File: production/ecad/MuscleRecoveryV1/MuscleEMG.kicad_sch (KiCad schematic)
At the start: 47 parts, among them J1 AudioJack3, J2 Screw_Terminal_01x03, J8 Screw_Terminal_01x07, U4 ADXL343, U5 AD8232ACPZ-R7, U7 ADS1115IDGS

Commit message: updated bom
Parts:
- C20, C21: footprint (none) -> Capacitor_SMD:C_0805_2012Metric
- R27, R65: footprint (none) -> Resistor_SMD:R_0805_2012Metric
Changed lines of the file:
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@@
       (effects (font (size 1.27 1.27)) (justify left))
     )
-    (property "Footprint" "" (at 149.86 146.05 0)
+    (property "Footprint" "Capacitor_SMD:C_0805_2012Metric" (at 149.86 146.05 0)
       (effects (font (size 1.27 1.27)) hide)
     )
@@
       (effects (font (size 1.27 1.27)) (justify left))
     )
-    (property "Footprint" "" (at 134.62 146.05 0)
+    (property "Footprint" "Capacitor_SMD:C_0805_2012Metric" (at 134.62 146.05 0)
       (effects (font (size 1.27 1.27)) hide)
     )
@@
     )
     (pin "1")
+    (pin "10")
+    (pin "11")
+    (pin "12")
+    (pin "13")
+    (pin "14")
+    (pin "2")
+    (pin "3")
+    (pin "4")
+    (pin "5")
+    (pin "6")
     (pin "7")
     (pin "8")
-    (pin "10")
-    (pin "2")
-    (pin "5")
     (pin "9")
-    (pin "13")
-    (pin "4")
-    (pin "14")
-    (pin "12")
-    (pin "11")
-    (pin "6")
-    (pin "3")
     (instances
       (project "MuscleRecoveryV1"
@@
       (effects (font (size 1.27 1.27)))
     )
-    (property "Footprint" "" (at 115.57 175.768 90)
+    (property "Footprint" "Resistor_SMD:R_0805_2012Metric" (at 115.57 175.768 90)
       (effects (font (size 1.27 1.27)) hide)
     )
@@
       (effects (font (size 1.27 1.27)))
     )
-    (property "Footprint" "" (at 115.57 173.228 90)
+    (property "Footprint" "Resistor_SMD:R_0805_2012Metric" (at 115.57 173.228 90)
       (effects (font (size 1.27 1.27)) hide)
     )
@@
       (effects (font (size 1.27 1.27)) hide)
     )
-    (pin "2")
-    (pin "1")
-    (instances
-      (project "MuscleRecoveryV1"
+    (pin "1")
+    (pin "2")
+    (instances
+      (project "MuscleRecoveryV1"

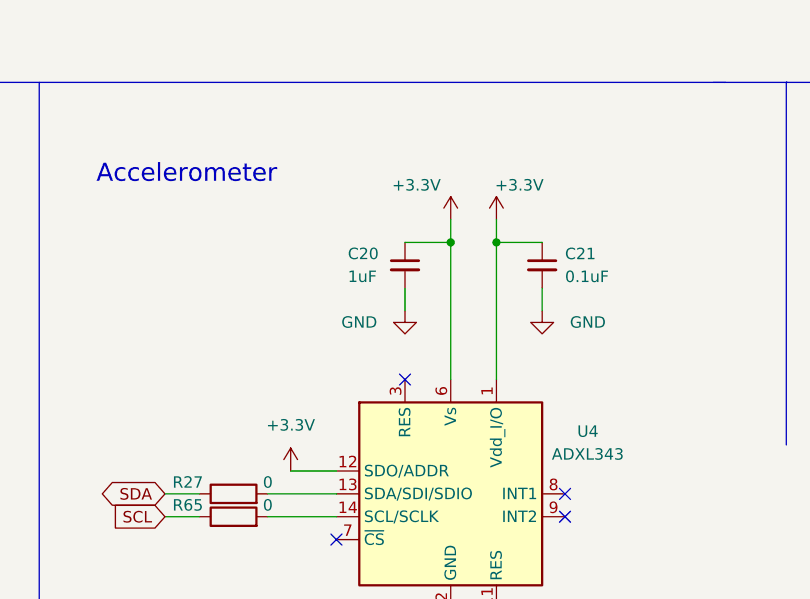
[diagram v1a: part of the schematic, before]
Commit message: added accelerometer to layout
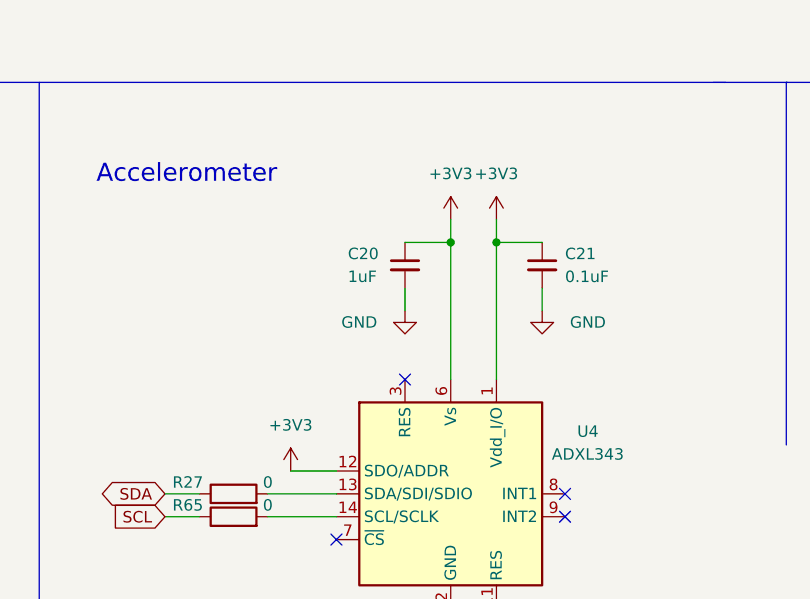
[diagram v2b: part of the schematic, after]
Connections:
- net +3.3V is gone; now on net +3V3: C20.1, C21.1, U4.1 (Vdd_I/O), U4.12 (SDO/ADDR), U4.6 (Vs)
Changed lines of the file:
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@@
-    )
-  )
-  (symbol (lib_id "power:+3.3V") (at 144.78 140.97 0) (unit 1)
-    (in_bom yes) (on_board yes) (dnp no)
-    (property "Reference" "#PWR073" (at 144.78 144.78 0)
-      (effects (font (size 1.27 1.27)) hide)
-    )
-    (property "Value" "+3.3V" (at 147.32 137.16 0)
-      (effects (font (size 1.27 1.27)))
-    )
-    (property "Footprint" "" (at 144.78 140.97 0)
-      (effects (font (size 1.27 1.27)) hide)
-    )
-    (property "Datasheet" "" (at 144.78 140.97 0)
-      (effects (font (size 1.27 1.27)) hide)
-    )
-    (pin "1")
-    (instances
-      (project "MuscleRecoveryV1"
-        (path "/4e550305-79d2-4e4a-a502-817ebcc79f9a/284c60dd-e199-4b03-b99f-cc7eaed256f8"
-          (reference "#PWR073") (unit 1)
-        )
-      )
     )
   )
@@
     )
   )
+  (symbol (lib_id "power:+3V3") (at 144.78 140.97 0) (unit 1)
+    (in_bom yes) (on_board yes) (dnp no) (fields_autoplaced)
+    (property "Reference" "#PWR072" (at 144.78 144.78 0)
+      (effects (font (size 1.27 1.27)) hide)
+    )
+    (property "Value" "+3V3" (at 144.78 135.89 0)
+      (effects (font (size 1.27 1.27)))
+    )
+    (property "Footprint" "" (at 144.78 140.97 0)
+      (effects (font (size 1.27 1.27)) hide)
+    )
+    (property "Datasheet" "" (at 144.78 140.97 0)
+      (effects (font (size 1.27 1.27)) hide)
+    )
+    (pin "1")
+    (instances
+      (project "MuscleRecoveryV1"
+        (path "/4e550305-79d2-4e4a-a502-817ebcc79f9a/284c60dd-e199-4b03-b99f-cc7eaed256f8"
+          (reference "#PWR072") (unit 1)
+        )
+      )
+    )
+  )
   (symbol (lib_id "Device:R") (at 100.33 74.93 90) (unit 1)
     (in_bom yes) (on_board yes) (dnp no)
@@
     )
   )
-  (symbol (lib_id "power:+3.3V") (at 139.7 140.97 0) (unit 1)
-    (in_bom yes) (on_board yes) (dnp no)
-    (property "Reference" "#PWR072" (at 139.7 144.78 0)
-      (effects (font (size 1.27 1.27)) hide)
-    )
-    (property "Value" "+3.3V" (at 135.89 137.16 0)
-      (effects (font (size 1.27 1.27)))
-    )
-    (property "Footprint" "" (at 139.7 140.97 0)
-      (effects (font (size 1.27 1.27)) hide)
-    )
-    (property "Datasheet" "" (at 139.7 140.97 0)
-      (effects (font (size 1.27 1.27)) hide)
-    )
-    (pin "1")
-    (instances
-      (project "MuscleRecoveryV1"
-        (path "/4e550305-79d2-4e4a-a502-817ebcc79f9a/284c60dd-e199-4b03-b99f-cc7eaed256f8"
-          (reference "#PWR072") (unit 1)
-        )
-      )
-    )
-  )
   (symbol (lib_id "Device:LED") (at 154.94 105.41 180) (unit 1)
     (in_bom yes) (on_board yes) (dnp no)
@@
         (path "/4e550305-79d2-4e4a-a502-817ebcc79f9a/284c60dd-e199-4b03-b99f-cc7eaed256f8"
           (reference "#PWR074") (unit 1)
-        )
-      )
-    )
-  )
-  (symbol (lib_id "power:+3.3V") (at 121.92 168.91 0) (unit 1)
-    (in_bom yes) (on_board yes) (dnp no) (fields_autoplaced)
-    (property "Reference" "#PWR038" (at 121.92 172.72 0)
-      (effects (font (size 1.27 1.27)) hide)
-    )
-    (property "Value" "+3.3V" (at 121.92 163.83 0)
-      (effects (font (size 1.27 1.27)))
-    )
-    (property "Footprint" "" (at 121.92 168.91 0)
-      (effects (font (size 1.27 1.27)) hide)
-    )
-    (property "Datasheet" "" (at 121.92 168.91 0)
-      (effects (font (size 1.27 1.27)) hide)
-    )
-    (pin "1")
-    (instances
-      (project "MuscleRecoveryV1"
-        (path "/4e550305-79d2-4e4a-a502-817ebcc79f9a/284c60dd-e199-4b03-b99f-cc7eaed256f8"
-          (reference "#PWR038") (unit 1)
         )
       )
@@
     )
   )
+  (symbol (lib_id "power:+3V3") (at 139.7 140.97 0) (unit 1)
+    (in_bom yes) (on_board yes) (dnp no) (fields_autoplaced)
+    (property "Reference" "#PWR038" (at 139.7 144.78 0)
+      (effects (font (size 1.27 1.27)) hide)
+    )
+    (property "Value" "+3V3" (at 139.7 135.89 0)
+      (effects (font (size 1.27 1.27)))
+    )
+    (property "Footprint" "" (at 139.7 140.97 0)
+      (effects (font (size 1.27 1.27)) hide)
+    )
+    (property "Datasheet" "" (at 139.7 140.97 0)
+      (effects (font (size 1.27 1.27)) hide)
+    )
+    (pin "1")
+    (instances
+      (project "MuscleRecoveryV1"
+        (path "/4e550305-79d2-4e4a-a502-817ebcc79f9a/284c60dd-e199-4b03-b99f-cc7eaed256f8"
+          (reference "#PWR038") (unit 1)
+        )
+      )
+    )
+  )
   (symbol (lib_id "Device:R") (at 111.76 74.93 90) (unit 1)
     (in_bom yes) (on_board yes) (dnp no)
@@
         )
       )
+    )
+  )
+  (symbol (lib_id "power:+3V3") (at 121.92 168.91 0) (unit 1)
+    (in_bom yes) (on_board yes) (dnp no) (fields_autoplaced)
+    (property "Reference" "#PWR073" (at 121.92 172.72 0)
+      (effects (font (size 1.27 1.27)) hide)
+    )
+    (property "Value" "+3V3" (at 121.92 163.83 0)
+      (effects (font (size 1.27 1.27)))
+    )
+    (property "Footprint" "" (at 121.92 168.91 0)
+      (effects (font (size 1.27 1.27)) hide)
+    )
+    (property "Datasheet" "" (at 121.92 168.91 0)
+      (effects (font (size 1.27 1.27)) hide)
+    )
+    (pin "1")
+    (instances
+      (project "MuscleRecoveryV1"
+        (path "/4e550305-79d2-4e4a-a502-817ebcc79f9a/284c60dd-e199-4b03-b99f-cc7eaed256f8"
+          (reference "#PWR073") (unit 1)
+        )
+      )
